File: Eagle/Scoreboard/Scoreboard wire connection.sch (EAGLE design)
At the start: 51 parts, among them X7 6ESRM-P

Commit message: Fixed connection plan, added pins
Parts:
- removed BTN_SETS, POWER: (no value), con-ptr500:AK300/2
- added 9V, BTN_POWER: (no value), con-ptr500:AK300/2
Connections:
- net 5V: now also 433MHZ_POWER-1.KL; no longer POWER-2.KL
- net GND: now also 12V_1-1.KL; no longer 12V_2-1.KL
- net N$57: now also SEGMENTS5-4.KL; no longer SEGMENTS5-1.KL
- net N$58: now also SEGMENTS5-5.KL; no longer SEGMENTS5-2.KL
- net N$59: now also SEGMENTS5-6.KL; no longer SEGMENTS5-3.KL
- net N$60: now also SEGMENTS5-7.KL; no longer SEGMENTS5-4.KL
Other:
- note added: "1"
- note added: "10"
- note added: "11"
- note added: "12"
- note added: "13"
- note added: "14"
- note added: "15"
- note added: "16"
- note added: "17"
- note added: "18"
- note added: "19"
- note added: "2"
- note added: "20"
- note added: "21"
- note added: "22"
- note added: "23"
- note added: "24"
- note added: "25"
- note added: "26"
- note added: "27"
- note added: "28"
- note added: "29"
- note added: "3"
- note added: "30"
- note added: "31"
- note added: "32"
- note added: "33"
- note added: "34"
- note added: "35"
- note added: "3V3"
- note added: "4"
- note added: "5"
- note added: "6"
- note added: "7"
- note added: "8"
- note added: "9"
- note added: "9V"
- note added: "A2"
- note added: "A3"
- note added: "A4"
- note added: "A5"
- note removed: "Pin 4"
- note removed: "Pin 5"
- note removed: "Pin 6"
- note removed: "Pin 7"
- note removed: "Pin 8"
- note removed: "Pin 9"
- note removed: "RESET"
- moved on the sheet: 433MHZ_POWER-1, 433MHZ_POWER-2, BLUETOOTH-1, BLUETOOTH-2, BLUETOOTH_POWER-1, BLUETOOTH_POWER-2, BTN_AWAY-1, BTN_AWAY-2, BTN_HOME-1, BTN_HOME-2, INFRA_POWER-1, INFRA_POWER-2

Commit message: Updated wiring
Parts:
- added 433_POWER, DATA, DATA1, DATA2, IR_POWER1, POWER: (no value), con-ptr500:AK300/2
- renumbered BTN_AWAY to DS3231, BTN_HOME to RES
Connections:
- new net N$61: DATA-2.KL, DS3231-2.KL
- new net N$62: DATA-1.KL, DS3231-1.KL
- new net N$63: 433_POWER-2.KL, INFRA_POWER-1.KL
- new net N$64: DATA1-2.KL, SIGNAL_IN-1.KL
- new net N$65: DATA2-2.KL, RES-1.KL
- net 5V: now also IR_POWER1-2.KL, POWER-1.KL
- net GND: now also IR_POWER1-1.KL, POWER-2.KL
- net N$53: now also 433_POWER-1.KL
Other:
- note added: "433 MHz Receiver"
- note added: "A3 433Mhz IN"
- note added: "A4 (SDA)"
- note added: "A5 (SCL)"
- note added: "IN"
- note added: "IR (HX1838)"
- note added: "RTC (DS3231)"
- note added: "SCL"
- note added: "SDA"
- note removed: "433MHz IN"
- note removed: "A3"
- note removed: "A4"
- note removed: "A5"

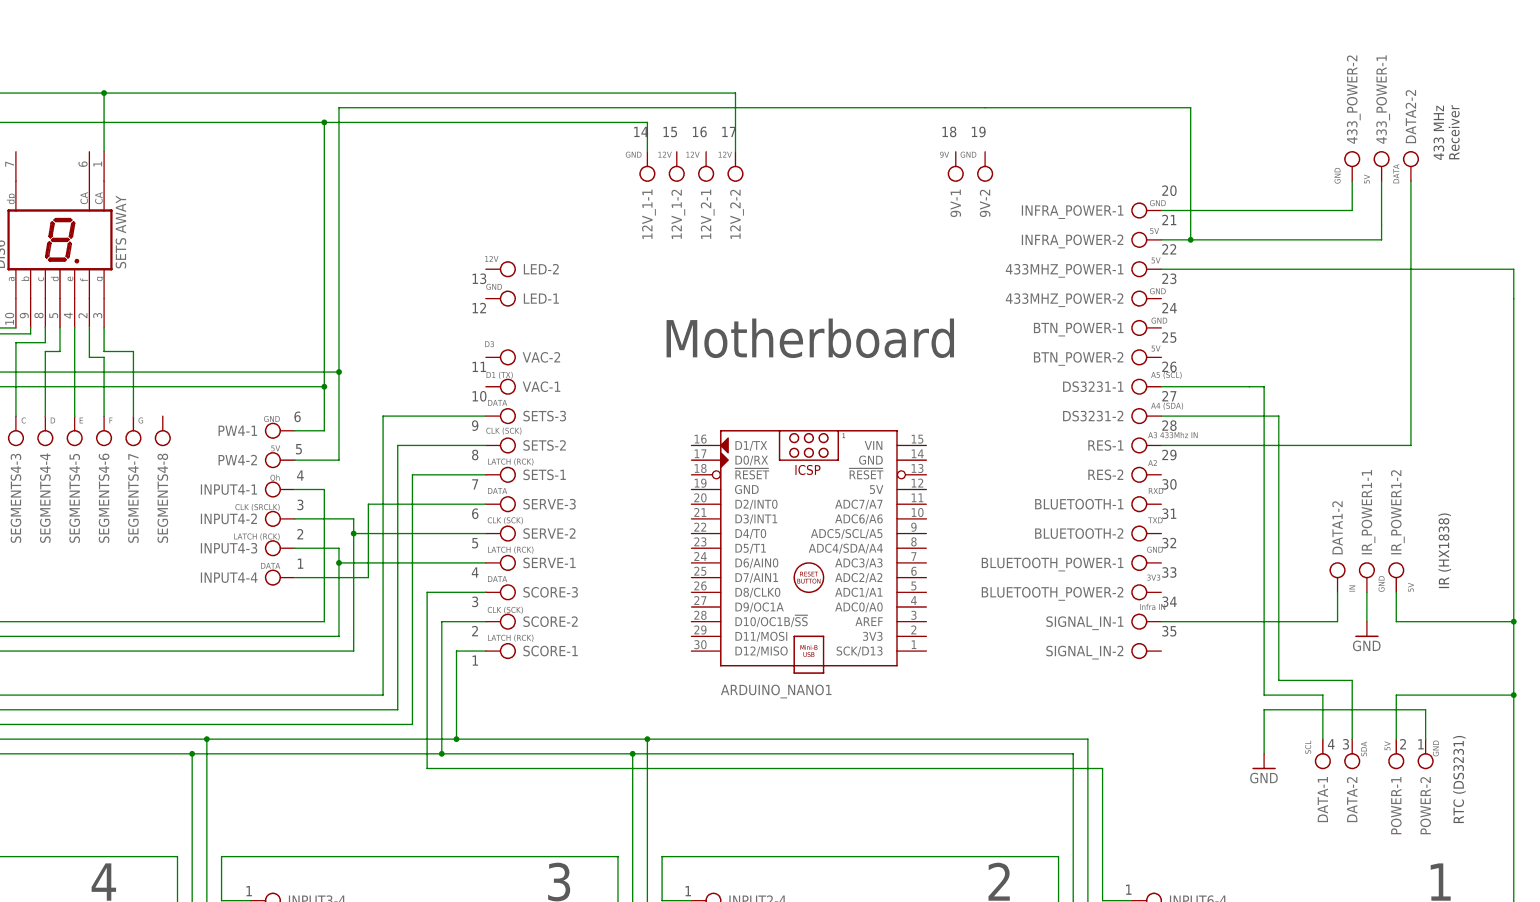
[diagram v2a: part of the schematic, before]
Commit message: Update wiring scheme to match real wirring with UNO
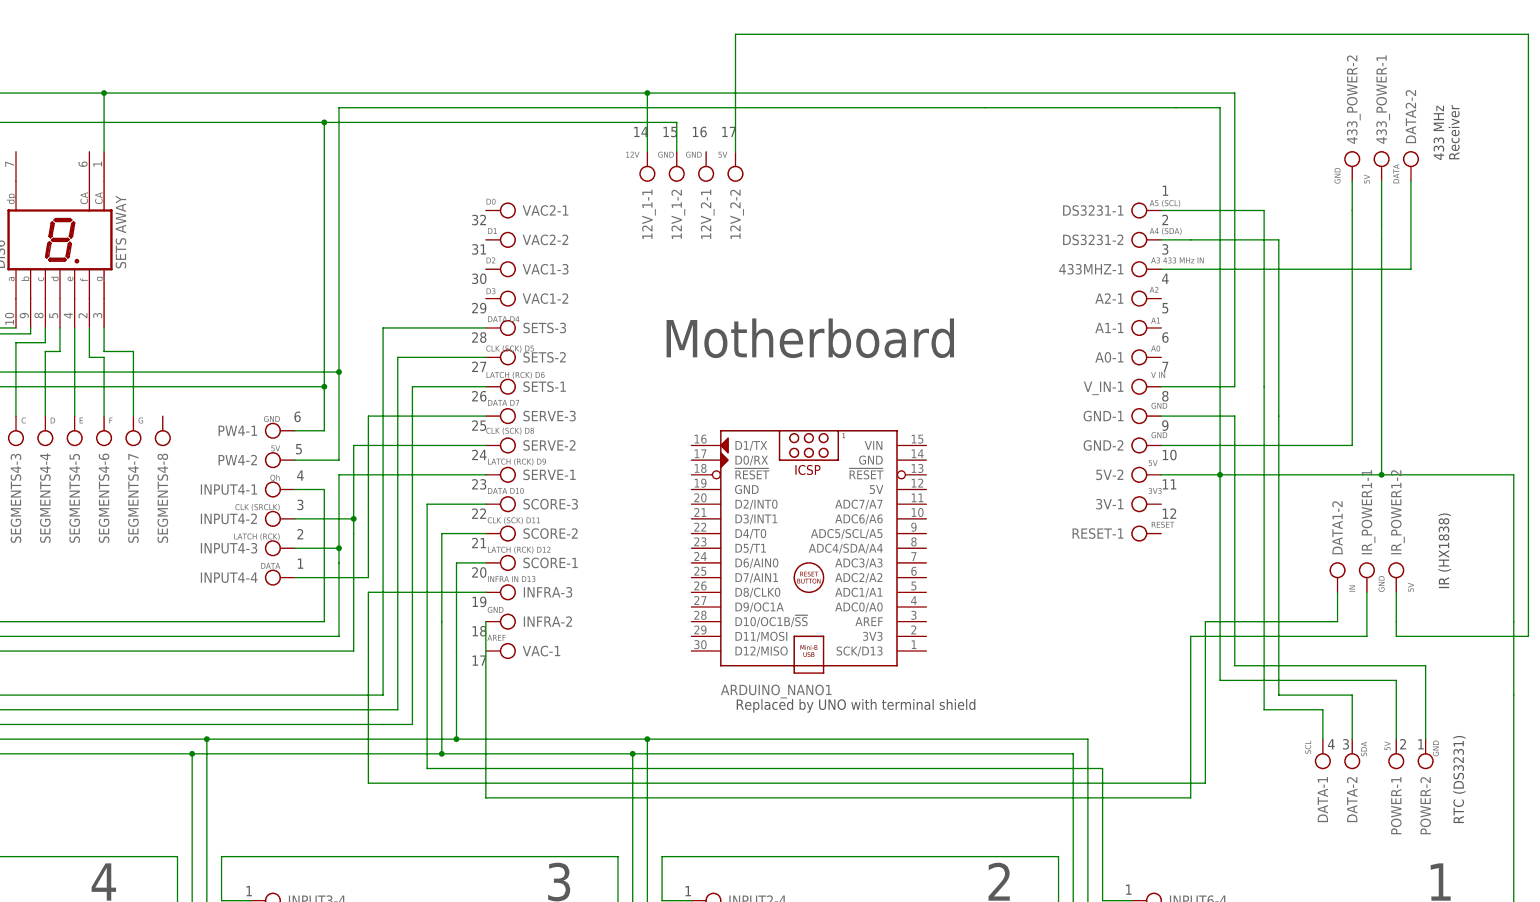
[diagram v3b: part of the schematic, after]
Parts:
- removed 9V, BLUETOOTH_POWER, INFRA_POWER, LED, RES, SIGNAL_IN: (no value), con-ptr500:AK300/2
- added 5V, A0, A2, GND, RESET, VAC2, V_IN: (no value), con-ptr500:AK300/2
- added INFRA, VAC1: (no value), con-ptr500:AK300/3
- VAC: device con-ptr500:AK300/3 -> con-ptr500:AK300/2
- renumbered 433MHZ_POWER to 433MHZ, BLUETOOTH to 3V, BTN_POWER to A1
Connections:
- removed net 5V: 433MHZ-1.KL, IR_POWER1-2.KL, POWER-1.KL, PW1-2.KL, PW2-2.KL, PW3-2.KL, PW5-2.KL, PW6-2.KL
- removed net N$63: 433_POWER-2.KL, INFRA_POWER-1.KL
- new net 433GND: 433_POWER-2.KL, GND-2.KL
- new net 5V1: 433_POWER-1.KL, 5V-2.KL, POWER-1.KL, PW-2.KL, PW1-2.KL, PW2-2.KL, PW3-2.KL, PW4-2.KL, PW5-2.KL, PW6-2.KL
- new net 5V_INFRA: 12V_2-2.KL, IR_POWER1-2.KL
- new net N$61: GND-1.KL, POWER-2.KL
- net 12V: now also 12V_1-1.KL, V_IN-1.KL; no longer 12V_2-2.KL
- net GND: now also 12V_1-2.KL; no longer 12V_1-1.KL, IR_POWER1-1.KL, POWER-2.KL
- net N$53: now also INFRA-2.KL, IR_POWER1-1.KL; no longer 433_POWER-1.KL, INFRA_POWER-2.KL, PW-2.KL, PW4-2.KL
- net N$64: now also INFRA-3.KL; no longer SIGNAL_IN-1.KL
- net N$65: now also 433MHZ-1.KL; no longer RES-1.KL
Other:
- note added: "A0"
- note added: "A1"
- note added: "A3 433 MHz IN"
- note added: "AREF"
- note added: "CLK (SCK) D11"
- note added: "CLK (SCK) D5"
- note added: "CLK (SCK) D8"
- note added: "D0"
- note added: "D1"
- note added: "D2"
- note added: "DATA D10"
- note added: "DATA D4"
- note added: "DATA D7"
- note added: "INFRA IN D13"
- note added: "LATCH (RCK) D12"
- note added: "LATCH (RCK) D6"
- note added: "LATCH (RCK) D9"
- note added: "RESET"
- note added: "Replaced by UNO with terminal shield"
- note added: "V IN"
- note removed: "13"
- note removed: "33"
- note removed: "34"
- note removed: "35"
- note removed: "9V"
- note removed: "A3 433Mhz IN"
- note removed: "CLK (SCK)"
- note removed: "D1 (TX)"
- note removed: "Infra IN"
- note removed: "RXD"
- note removed: "TXD"
- moved on the sheet: DS3231-1, DS3231-2, SCORE-1, SCORE-2, SCORE-3, SERVE-1, SERVE-2, SERVE-3, SETS-1, SETS-2, SETS-3, VAC-1
